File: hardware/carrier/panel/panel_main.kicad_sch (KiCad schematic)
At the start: 28 parts, among them J1 GDEY029T94 FPC, J2 CARRIER, J3 FL-A FPC (FL03), J4 FL-B FPC (Orient), Q5 SI1308EDL

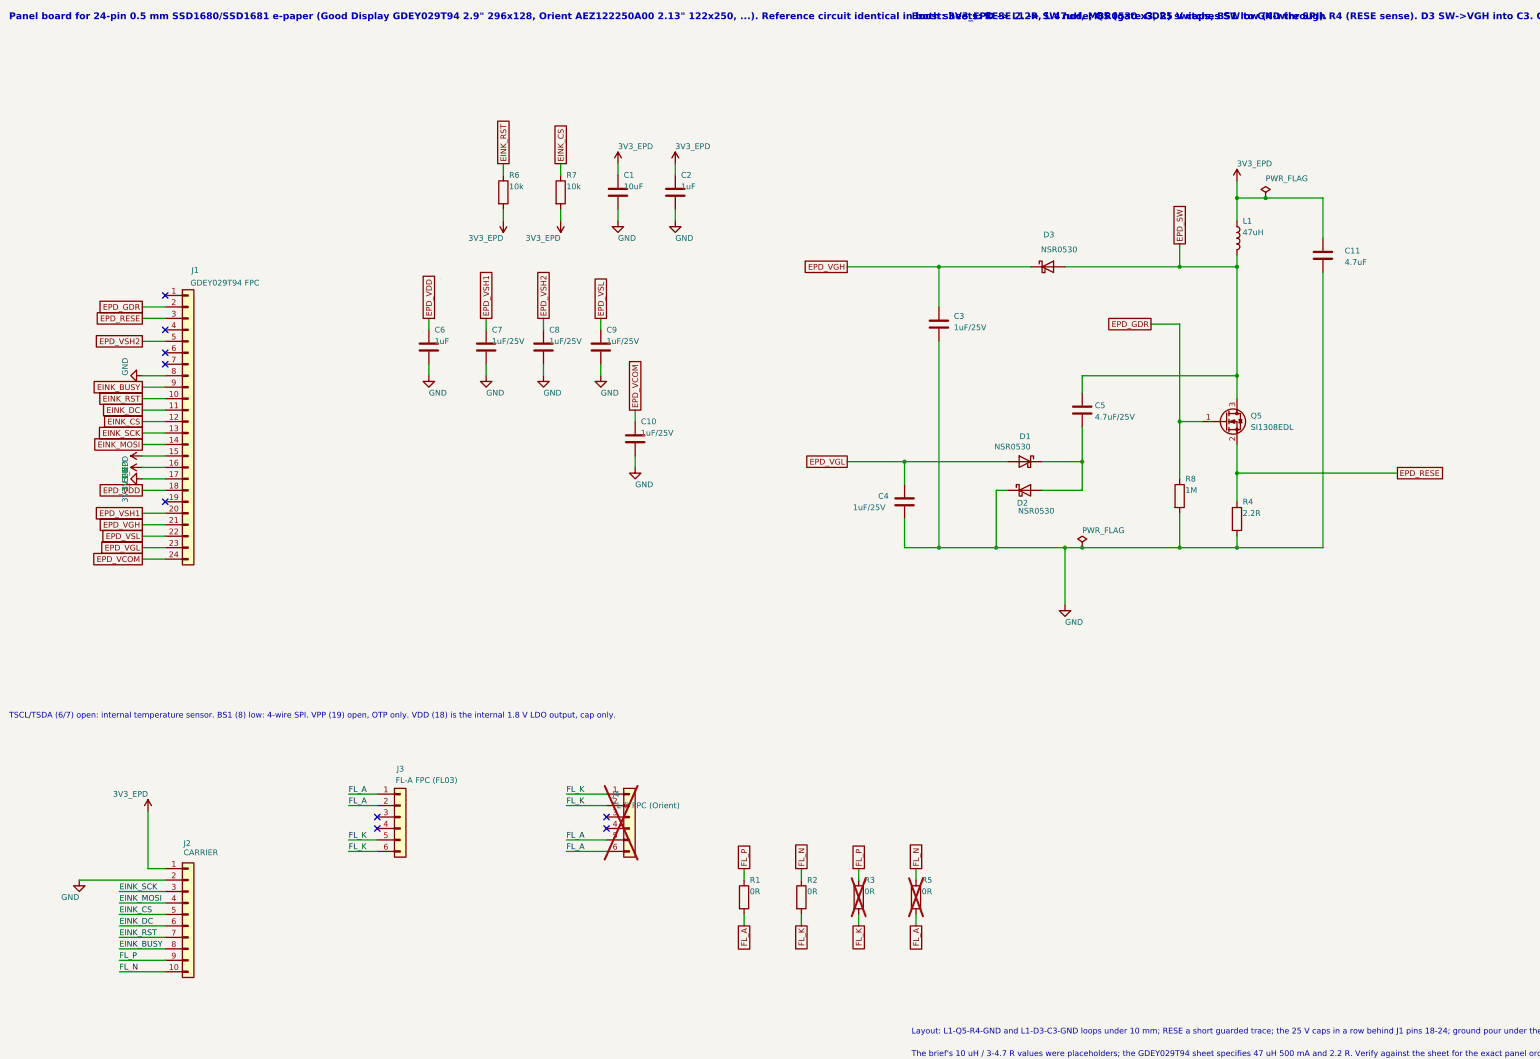
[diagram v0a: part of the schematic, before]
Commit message: Carrier v0.2c WIP: cassette screw holes, top-actuated SW2, wider board, panel schematic fixes
Work in progress for the 3D-printed display cassette; routing is DRC-clean
(0 errors) with 14 signal links and 3 ground islands left for hand finishing
(list in HANDOFF-v0.2.md).

Carrier:
- H1-H3 M2 cassette screw holes (2.2 mm NPTH, 4.5 mm copper-free annulus on
  both layers via footprint rule areas + per-hole DRC rules) at (77.4, 60.9),
  (111.2, 59.95), (111.2, 105.85); schematic symbols in the core sheet.
- SW2 power switch -> C&K JS102011SAQN top-actuated SPDT (LCSC C221660),
  travel along X; top strip is now J6, SW1, SW2 (x 80.0..108.5).
- Board widened to x 120.5 so the right-side holes fit beside the header
  column (J2 keyboard header stays topmost, cable into the plate channel).
- F.Fab note to trim the Walter header pins flush; stale KBD label moved.
- 3D models added: JS102011SAQN, MAX17048 (U6), JST PH S2B-PH-SM4-TB (J7);
  STEP export in out/ for the Fusion assembly.
- Owner's manual schematic edits (test points) included.

Panel:
- Owner's rearranged panel_main.kicad_sch with the EPD_GDR wire gap closed
  (J1 pin 2 back on the boost gate net); both front-light FPC connectors kept.

Co-Authored-By: Claude Fable 5.1 <noreply@anthropic.com>
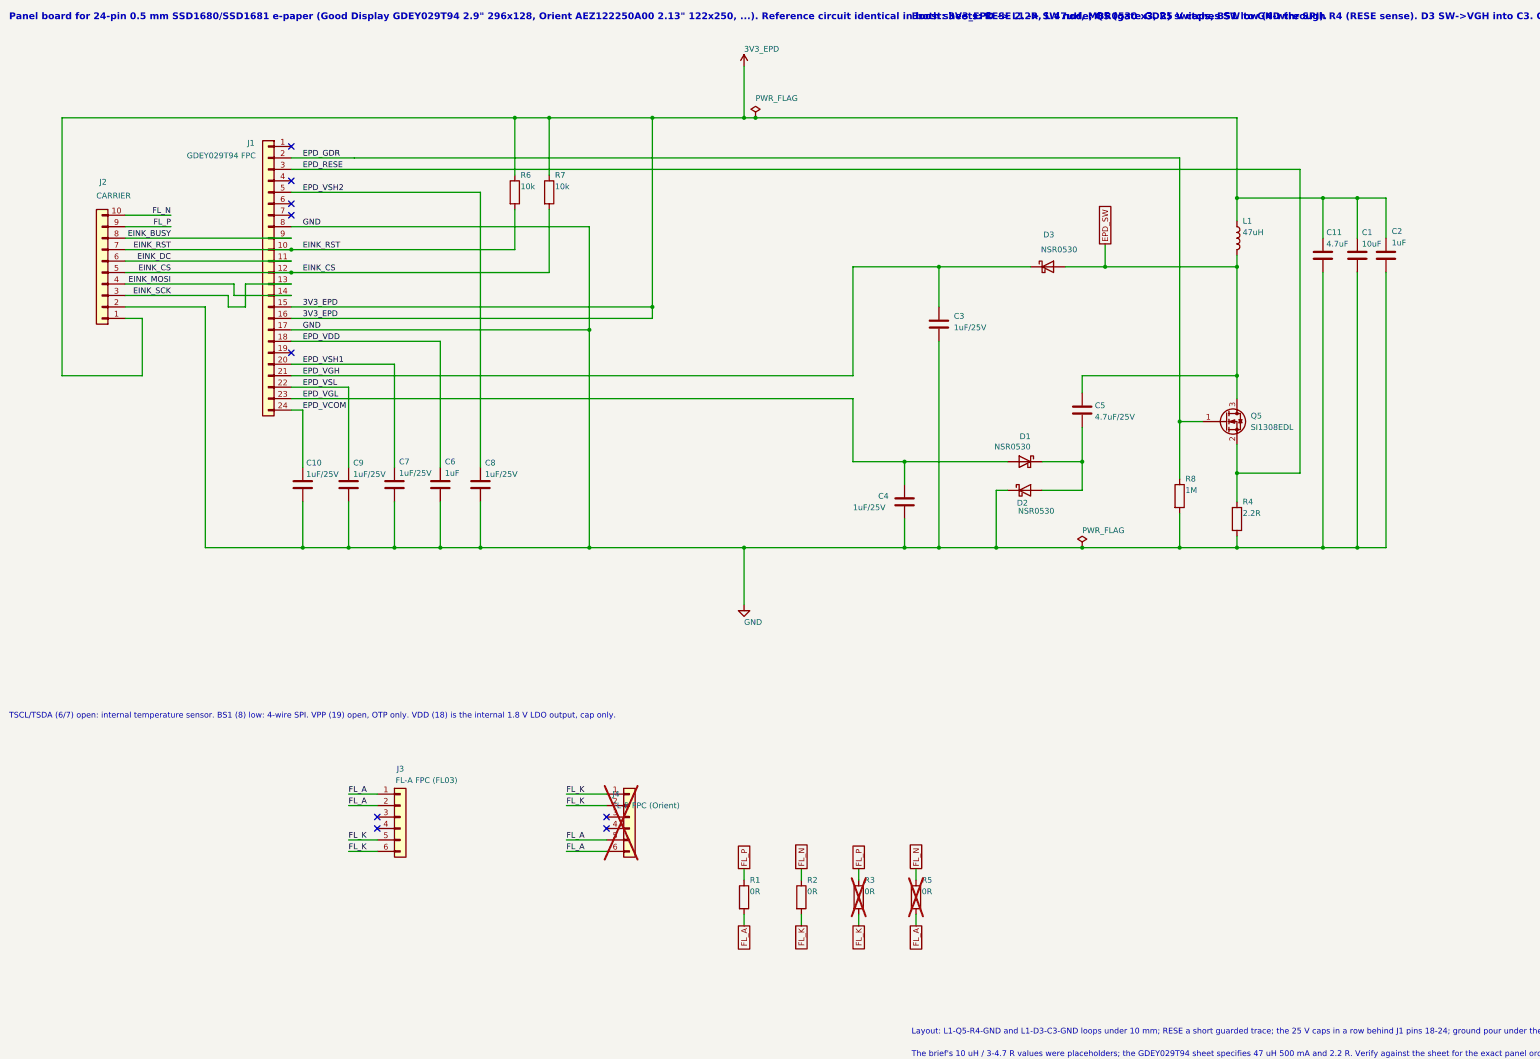
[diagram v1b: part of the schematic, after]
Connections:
- net 3V3_EPD: now also R6.1, R7.1; no longer R6.2, R7.2
- net EINK_CS: now also R7.2; no longer R7.1
- net EINK_RST: now also R6.2; no longer R6.1
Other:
- moved on the sheet: C10, C6, C7, C8, C9, J1, J2, R6, R7

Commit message: BOM: move six passives to JLC basic parts, fix connector LCSC codes (no footprint changes)
Carrier: R32 2.2M -> 1M (C26083), C14 22nF -> 100nF (C1525), R1 22.1k -> 22k (C25768),
R2 47.5k -> 47k (C25792); J1 LCSC C160407 (SM08B), J2 MPN/LCSC SM04B-SRSS-TB C160404
to match its SH footprint.
Panel: C11 4.7uF under basic code C19666, D1-D3 NSR0530 -> B5819W (C8598, SOD-123 as
already on the board), R4 2.2R gets C22939.
Board footprint fields updated to match. ERC clean on both.

Co-Authored-By: Claude Fable 5.1 <noreply@anthropic.com>
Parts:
- C11: LCSC C1705 -> C19666
- D1, D2, D3: value NSR0530 -> B5819W; footprint Diode_SMD:D_SOD-323 -> Diode_SMD:D_SOD-123; LCSC C556393 -> C8598; MPN NSR0530HT1G -> B5819W
- R4: LCSC (none) -> C22939
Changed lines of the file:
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@@
 			)
 		)
-		(property "LCSC" ""
+		(property "LCSC" "C22939"
 			(at 292.1 149.86 0)
 			(hide yes)
@@
 			)
 		)
-		(property "Value" "NSR0530"
+		(property "Value" "B5819W"
 			(at 246.38 116.078 0)
 			(show_name no)
@@
 			)
 		)
-		(property "Footprint" "Diode_SMD:D_SOD-323"
+		(property "Footprint" "Diode_SMD:D_SOD-123"
 			(at 240.03 123.19 0)
 			(hide yes)
@@
 			)
 		)
-		(property "MPN" "NSR0530HT1G"
+		(property "MPN" "B5819W"
 			(at 245.11 134.62 0)
 			(hide yes)
@@
 			)
 		)
-		(property "LCSC" "C556393"
+		(property "LCSC" "C8598"
 			(at 245.11 137.16 0)
 			(hide yes)
@@
 			)
 		)
-		(property "Value" "NSR0530"
+		(property "Value" "B5819W"
 			(at 243.586 130.302 0)
 			(show_name no)
@@
 			)
 		)
-		(property "Footprint" "Diode_SMD:D_SOD-323"
+		(property "Footprint" "Diode_SMD:D_SOD-123"
 			(at 250.19 129.54 0)
 			(hide yes)
@@
 			)
 		)
-		(property "MPN" "NSR0530HT1G"
+		(property "MPN" "B5819W"
 			(at 245.11 140.97 0)
 			(hide yes)
@@
 			)
 		)
-		(property "LCSC" "C556393"
+		(property "LCSC" "C8598"
 			(at 245.11 143.51 0)
 			(hide yes)
@@
 			)
 		)
-		(property "LCSC" "C1705"
+		(property "LCSC" "C19666"
 			(at 311.15 91.44 0)
 			(hide yes)
@@
 			)
 		)
-		(property "Value" "NSR0530"
+		(property "Value" "B5819W"
 			(at 248.666 72.39 0)
 			(show_name no)
@@
 			)
 		)
-		(property "Footprint" "Diode_SMD:D_SOD-323"
+		(property "Footprint" "Diode_SMD:D_SOD-123"
 			(at 255.27 80.01 0)
 			(hide yes)
@@
 			)
 		)
-		(property "MPN" "NSR0530HT1G"
+		(property "MPN" "B5819W"
 			(at 250.19 91.44 0)
 			(hide yes)
@@
 			)
 		)
-		(property "LCSC" "C556393"
+		(property "LCSC" "C8598"
 			(at 250.19 93.98 0)
 			(hide yes)

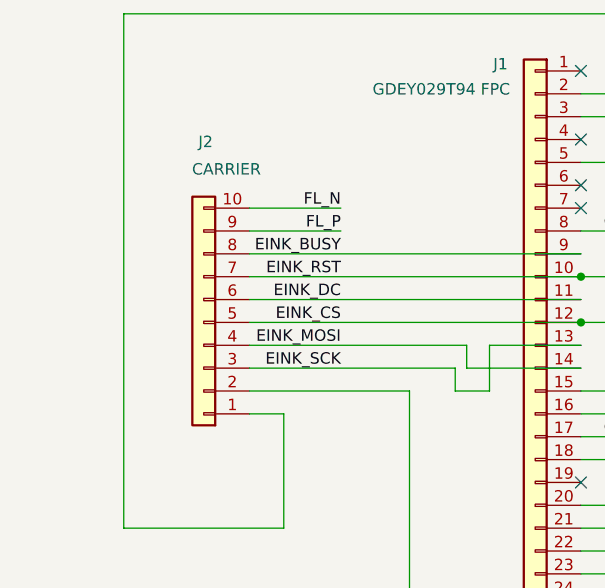
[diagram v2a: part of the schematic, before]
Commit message: Panel: split the frontlight off the carrier cable (J2 -> 8-pin SH, new J5 2-pin), re-routed
Schematic: J2 CARRIER is SM08B-SRSS-TB (C160407) on the same wires; new J5 FRONTLIGHT
SM02B-SRSS-TB (C160402) takes FL_P (pin 1) and FL_N (pin 2), matching carrier J8.
Board: J2 swapped with pins 1-8 in place, J5 at the bottom-left corner, R7 nudged,
full Freerouting pass (0 unrouted), GND pours refilled.
Known: 25 tracks below the 0.2 mm minimum width, J5 mounting pads 0.2 mm too close to
the bottom edge; owner finishing by hand.

Co-Authored-By: Claude Fable 5.1 <noreply@anthropic.com>
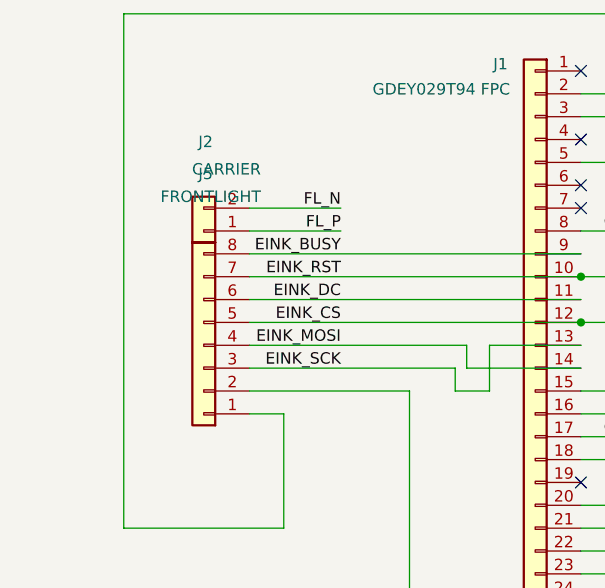
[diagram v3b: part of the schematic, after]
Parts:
- added J5: FRONTLIGHT, Connector_JST:JST_SH_SM02B-SRSS-TB_1x02-1MP_P1.00mm_Horizontal, symbol Connector_Generic:Conn_01x02
- J2: footprint Connector_JST:JST_SH_SM10B-SRSS-TB_1x10-1MP_P1.00mm_Horizontal -> Connector_JST:JST_SH_SM08B-SRSS-TB_1x08-1MP_P1.00mm_Horizontal; symbol Connector_Generic:Conn_01x10 -> Connector_Generic:Conn_01x08; LCSC C160409 -> C160407; MPN SM10B-SRSS-TB -> SM08B-SRSS-TB
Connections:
- net FL_N: now also J5.2 (Pin_2); no longer J2.10 (Pin_10)
- net FL_P: now also J5.1 (Pin_1); no longer J2.9 (Pin_9)
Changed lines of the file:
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@@
 	)
 	(symbol
-		(lib_id "Connector_Generic:Conn_01x10")
-		(at 40.64 77.47 180)
+		(lib_id "Connector_Generic:Conn_01x08")
+		(at 40.64 80.01 180)
 		(unit 1)
 		(body_style 1)
@@
 			)
 		)
-		(property "Footprint" "Connector_JST:JST_SH_SM10B-SRSS-TB_1x10-1MP_P1.00mm_Horizontal"
+		(property "Footprint" "Connector_JST:JST_SH_SM08B-SRSS-TB_1x08-1MP_P1.00mm_Horizontal"
 			(at 44.45 82.55 0)
 			(hide yes)
@@
 			)
 		)
-		(property "Description" "Generic connector, single row, 01x10, script generated (kicad-library-utils/schlib/autogen/connector/)"
+		(property "Description" "Generic connector, single row, 01x08, script generated (kicad-library-utils/schlib/autogen/connector/)"
 			(at 44.45 77.47 0)
 			(hide yes)
@@
 			)
 		)
-		(property "MPN" "SM10B-SRSS-TB"
+		(property "MPN" "SM08B-SRSS-TB"
 			(at 40.64 62.23 0)
 			(hide yes)
@@
 			)
 		)
-		(property "LCSC" "C160409"
+		(property "LCSC" "C160407"
 			(at 40.64 59.69 0)
 			(hide yes)
@@
 		)
 		(pin "8"
-		)
-		(pin "9"
-		)
-		(pin "10"
 		)
 		(instances
@@
 					(unit 1)
 				)
+			)
+		)
+	)
+	(symbol
+		(lib_id "Connector_Generic:Conn_01x02")
+		(at 40.64 67.31 180)
+		(unit 1)
+		(body_style 1)
+		(exclude_from_sim no)
+		(in_bom yes)
+		(on_board yes)
+		(in_pos_files yes)
+		(dnp no)
+		(property "Reference" "J5"
+			(at 41.656 60.96 0)
+			(show_name no)
+			(do_not_autoplace no)
+			(effects
+				(font
+					(size 1.27 1.27)
+				)
+				(justify left)
+			)
+		)
+		(property "Value" "FRONTLIGHT"
+			(at 46.99 63.5 0)
+			(show_name no)
+			(do_not_autoplace no)
+			(effects
+				(font
+					(size 1.27 1.27)
+				)
+				(justify left)
+			)
+		)
+		(property "Footprint" "Connector_JST:JST_SH_SM02B-SRSS-TB_1x02-1MP_P1.00mm_Horizontal"
+			(at 44.45 82.55 0)
+			(hide yes)
+			(show_name no)
+			(do_not_autoplace no)
+			(effects
+				(font
+					(size 1.27 1.27)
+				)
+				(justify left)
+			)
+		)
+		(property "Datasheet" "~"
+			(at 44.45 80.01 0)
+			(hide yes)
+			(show_name no)
+			(do_not_autoplace no)
+			(effects
+				(font
+					(size 1.27 1.27)
+				)
+				(justify left)
+			)
+		)
+		(property "Description" "Generic connector, single row, 01x02, script generated (kicad-library-utils/schlib/autogen/connector/)"
+			(at 44.45 77.47 0)
+			(hide yes)
+			(show_name no)
+			(do_not_autoplace no)
+			(effects
+				(font
+					(size 1.27 1.27)
+				)
+				(justify left)
+			)
+		)
+		(property "MPN" "SM02B-SRSS-TB"
+			(at 40.64 62.23 0)
+			(hide yes)
+			(show_name no)
+			(do_not_autoplace no)
+			(effects
+				(font
+					(size 1.27 1.27)
+				)
+			)
+		)
+		(property "LCSC" "C160402"
+			(at 40.64 59.69 0)
+			(hide yes)
+			(show_name no)
+			(do_not_autoplace no)
+			(effects
+				(font
+					(size 1.27 1.27)
+				)
+			)
+		)
+		(property "DNP" ""
+			(at 40.64 57.15 0)
+			(hide yes)
+			(show_name no)
+			(do_not_autoplace no)
+			(effects
+				(font
+					(size 1.27 1.27)
+				)
+			)
+		)
+		(property "Note" "to carrier J3, 1:1 10-way SH cable"
+			(at 40.64 54.61 0)
+			(hide yes)
+			(show_name no)
+			(do_not_autoplace no)
+			(effects
+				(font
+					(size 1.27 1.27)
+				)
+			)
+		)
+		(pin "1"
+		)
+		(pin "2"
+		)
+		(instances
+			(project "pager-panel"
+				(path "/a764166a-207c-5736-a7df-1b396ea4a3e6/4abcc5ec-0e62-56fc-ae53-06c7680dbff6"
+					(reference "J5")
+					(unit 1)
+				)
